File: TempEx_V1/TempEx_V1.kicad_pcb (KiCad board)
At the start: 2 copper layers, 25 parts, among them J1 Conn_01x02, J2 Conn_01x10, J3 Conn_01x02, J4 Conn_01x02, J5 Conn_01x02, U1 MAX31865xTP, U2 MAX31865xTP, U3 MAX31865xTP, U4 MAX31865xTP

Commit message: WIP
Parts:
- moved C4 95.2 mm to (145.2, 118.8), turned to -90 degrees
- moved C3 94.8 mm to (145.2, 115.4), turned to 90 degrees
- moved J3 93.4 mm to (137.6, 111.1), turned to 180 degrees
- moved U2 91.0 mm to (141.3, 117.4), turned to -90 degrees
- moved C10 90.4 mm to (137.4, 117.3), turned to -90 degrees
- moved R2 89.2 mm to (141.6, 113.8), turned to 180 degrees
- moved J1 74.8 mm to (117.7, 111.2), turned to 180 degrees
- moved C1 72.3 mm to (125.2, 115.4), turned to 90 degrees
- moved C2 71.9 mm to (125.2, 118.8), turned to -90 degrees
- moved J5 68.4 mm to (142.3, 138.8)
- moved R4 68.1 mm to (138.4, 136.2)
- moved R1 65.4 mm to (121.6, 113.8), turned to 180 degrees
- moved C12 63.8 mm to (142.6, 132.6), turned to 90 degrees
- moved C7 63.7 mm to (134.8, 134.6), turned to -90 degrees
- moved C9 63.3 mm to (117.4, 117.4), turned to -90 degrees
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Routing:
- net +3V3: track 0.00 -> 176.8 mm
- net /Temperature/SPI_MOSI: track 0.00 -> 63.0 mm, vias 0 -> 4
- net /Temperature/SPI_NSS1: track 0.00 -> 56.9 mm
- net /Temperature/SPI_MISO: track 0.00 -> 55.4 mm, vias 0 -> 6
- net /Temperature/SPI_CLK: track 0.00 -> 55.0 mm, vias 0 -> 5
- net /Temperature/SPI_NSS2: track 0.00 -> 40.1 mm, vias 0 -> 2
- net /Temperature/SPI_NSS4: track 0.00 -> 35.8 mm
- net GND: track 0.00 -> 35.7 mm, vias 0 -> 8
- net /Temperature/SPI_NSS3: track 0.00 -> 18.8 mm
- net Net-(C11-Pad1): track 0.00 -> 11.9 mm
- net Net-(C10-Pad1): track 0.00 -> 11.9 mm
- net Net-(C9-Pad1): track 0.00 -> 11.8 mm
- net Net-(C12-Pad1): track 0.00 -> 11.8 mm
- net Net-(C11-Pad2): track 0.00 -> 10.7 mm
- net GNDD: track 0.00 -> 10.7 mm
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- added copper zone on B.Cu, net GND
- added copper zone on F.Cu, net GND
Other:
- board outline added: 50 x 40 mm
- board text added: "Temp1"
- board text added: "Temp2"
- board text added: "Temp3"
- board text added: "Temp4"

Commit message: GNDD Problem still unresolved
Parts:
- R1, R2, R3, R4: footprint Resistor_SMD:R_0201_0603Metric_Pad0.64x0.40mm_HandSolder -> Resistor_SMD:R_0603_1608Metric_Pad0.98x0.95mm_HandSolder
- moved R3 0.93 mm to (117.5, 136.6)
- moved R4 0.84 mm to (137.6, 136.5)
- moved R1 0.80 mm to (122.3, 113.5)
- moved R2 0.79 mm to (142.3, 113.5)
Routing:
- net +3V3: track 176.8 -> 175.5 mm
- net Net-(R3-Pad1): track 1.84 -> 2.52 mm
- net Net-(C9-Pad2): track 10.1 -> 10.7 mm
- net Net-(R4-Pad1): track 1.83 -> 2.43 mm
- net Net-(R2-Pad1): track 1.84 -> 2.43 mm
- net Net-(R1-Pad1): track 1.84 -> 2.41 mm
- net GND: vias 8 -> 12

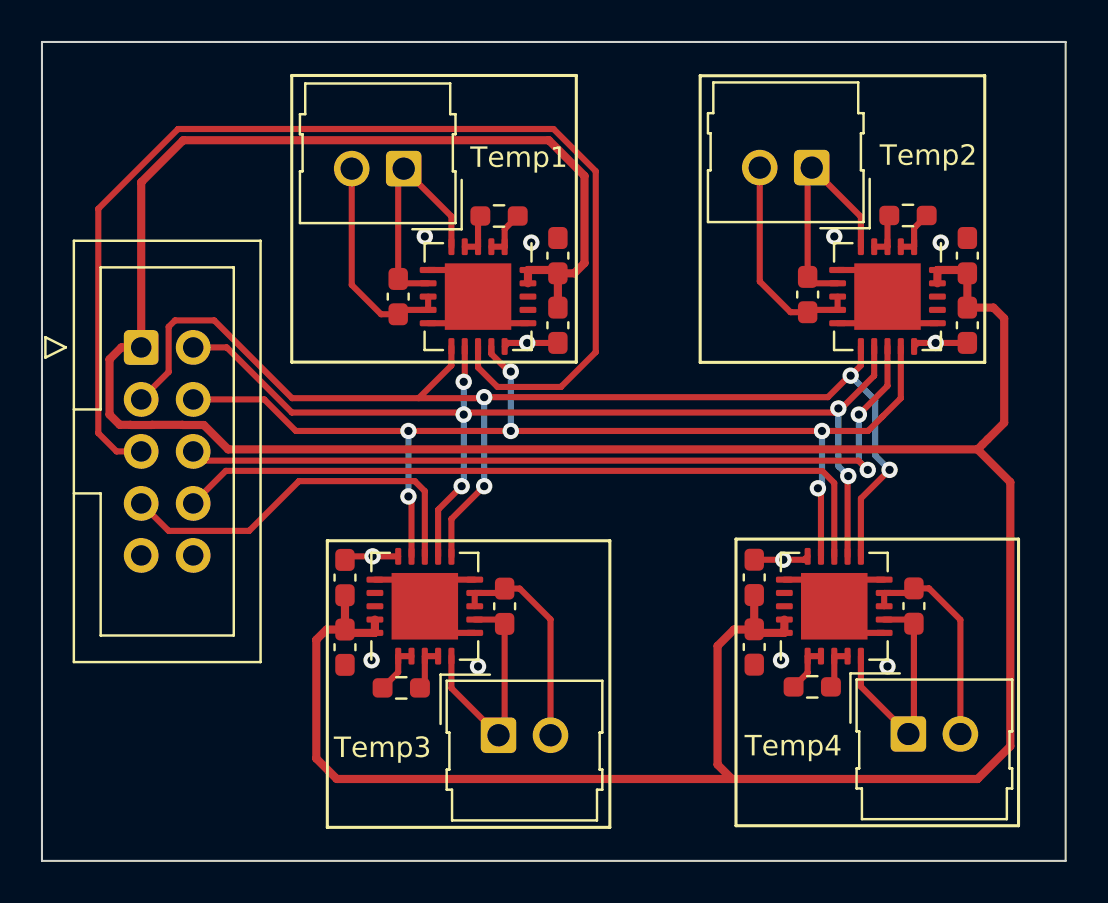
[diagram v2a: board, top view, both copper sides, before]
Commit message: Stitching missing
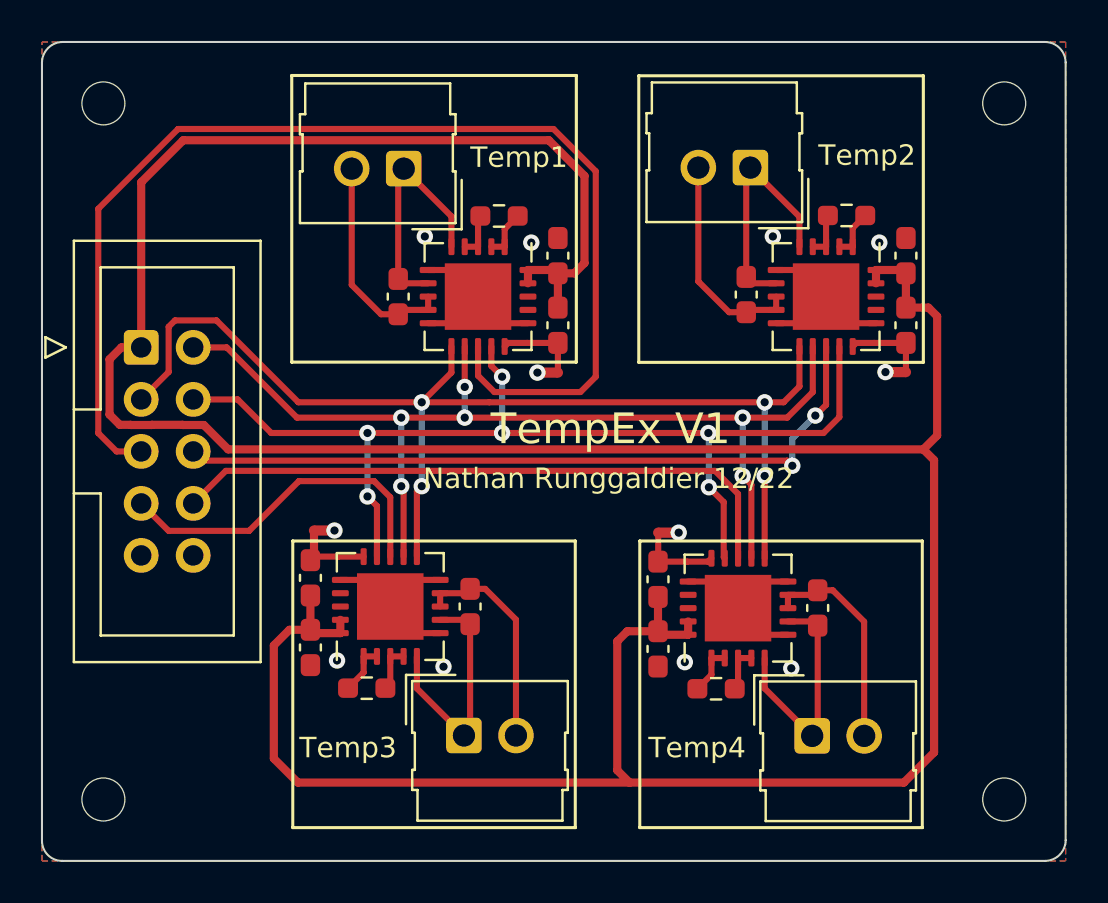
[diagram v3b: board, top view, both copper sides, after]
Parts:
- added H1: MountingHole, MountingHole:MountingHole_2.1mm, F.Cu at (103.0, 108.0)
- added H2: MountingHole, MountingHole:MountingHole_2.1mm, F.Cu at (103.0, 142.0)
- added H3: MountingHole, MountingHole:MountingHole_2.1mm, F.Cu at (147.0, 142.0)
- added H4: MountingHole, MountingHole:MountingHole_2.1mm, F.Cu at (147.0, 108.0)
- added NT1: NetTie_2, NetTie:NetTie-2_SMD_Pad0.5mm, F.Cu at (124.7, 121.2)
- added NT2: NetTie_2, NetTie:NetTie-2_SMD_Pad0.5mm, F.Cu at (141.7, 121.1)
- added NT3: NetTie_2, NetTie:NetTie-2_SMD_Pad0.5mm, F.Cu at (113.8, 128.9)
- added NT4: NetTie_2, NetTie:NetTie-2_SMD_Pad0.5mm, F.Cu at (130.6, 129.0)
- moved C12 4.70 mm to (137.9, 132.6)
- moved C7 4.70 mm to (130.1, 134.6)
- moved C8 4.70 mm to (130.1, 131.2)
- moved J5 4.70 mm to (137.6, 138.9)
- moved R4 4.70 mm to (132.9, 136.6)
- moved U4 4.70 mm to (134.0, 132.7)
- moved C10 3.00 mm to (134.4, 117.3)
- moved C3 3.00 mm to (142.2, 115.4)
- moved C4 3.00 mm to (142.2, 118.8)
- moved J3 3.00 mm to (134.6, 111.1)
- moved R2 3.00 mm to (139.3, 113.5)
- moved U2 3.00 mm to (138.3, 117.4)
- moved C11 1.69 mm to (120.9, 132.6)
- moved C5 1.69 mm to (113.1, 134.6)
- moved C6 1.69 mm to (113.1, 131.2)
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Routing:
- net GNDD: track 10.7 -> 16.3 mm
- net /Temperature/SPI_MOSI: track 63.0 -> 57.6 mm
- net /Temperature/SPI_NSS4: track 35.8 -> 30.9 mm
- net +3V3: track 175.5 -> 171.3 mm
- net /Temperature/SPI_NSS2: track 40.1 -> 36.1 mm
- net /Temperature/SPI_CLK: track 55.0 -> 51.8 mm, vias 5 -> 6
- net /Temperature/SPI_MISO: track 55.4 -> 53.1 mm
- net /Temperature/SPI_NSS3: track 18.8 -> 17.0 mm
- net /Temperature/SPI_NSS1: track 56.9 -> 58.0 mm
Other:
- outline, holes or cut-outs redrawn
- board text added: "Nathan Runggaldier 12/22"
- board text added: "TempEx V1"

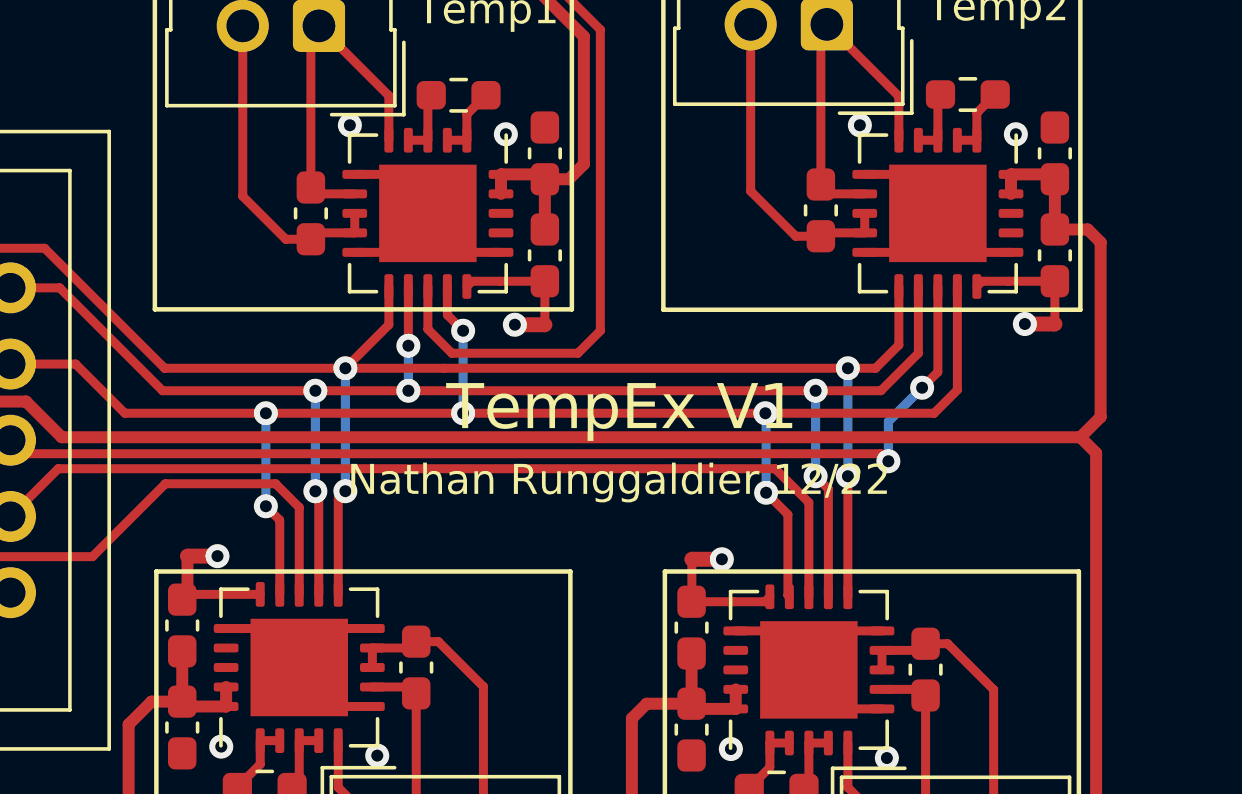
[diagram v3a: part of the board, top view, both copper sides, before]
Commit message: Updated GND
All GNDD switched to GND
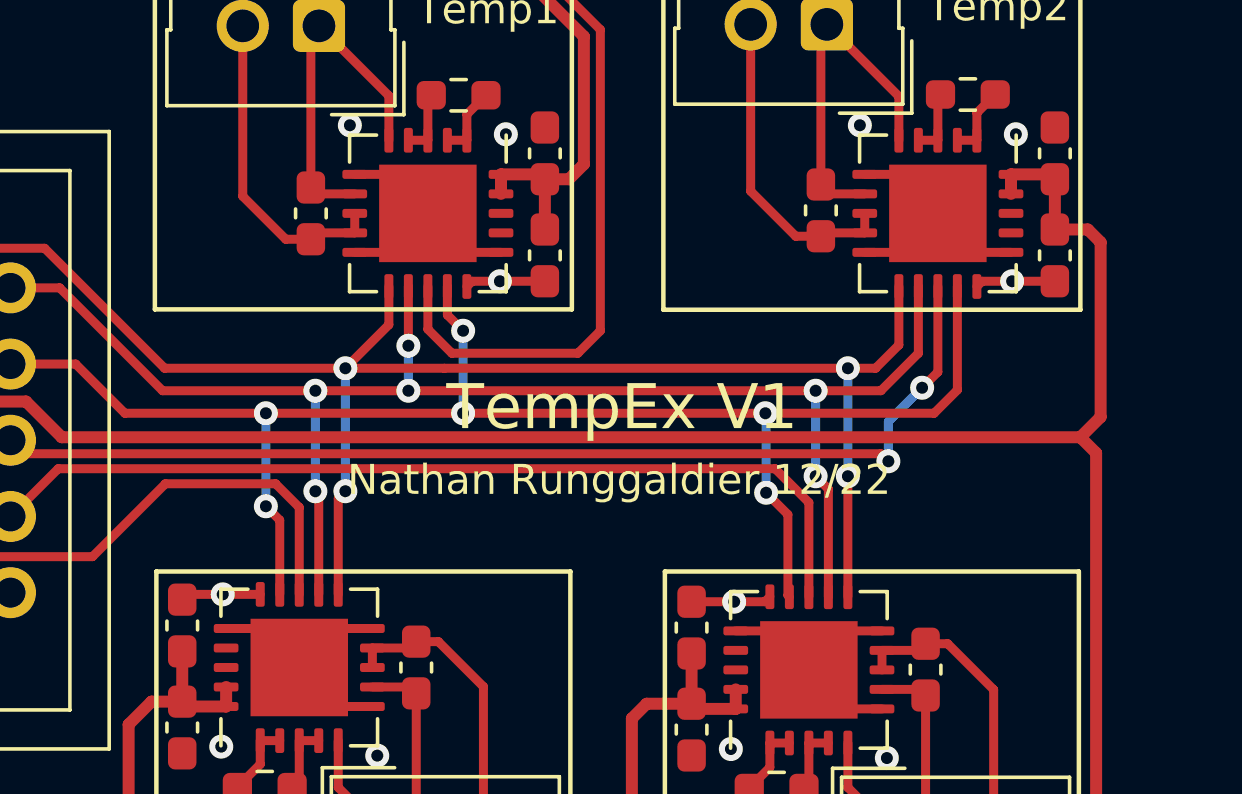
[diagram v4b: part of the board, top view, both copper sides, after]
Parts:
- removed NT1, NT2, NT3, NT4: NetTie_2, NetTie:NetTie-2_SMD_Pad0.5mm
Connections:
- C2 pad 2: GNDD -> GND
- C4 pad 2: GNDD -> GND
- C6 pad 2: GNDD -> GND
- C8 pad 2: GNDD -> GND
- U1 pad 15: GNDD -> GND
- U2 pad 15: GNDD -> GND
- U3 pad 15: GNDD -> GND
- U4 pad 15: GNDD -> GND
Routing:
- net GNDD: track 16.3 -> 0.00 mm
- net GND: track 35.7 -> 46.4 mm

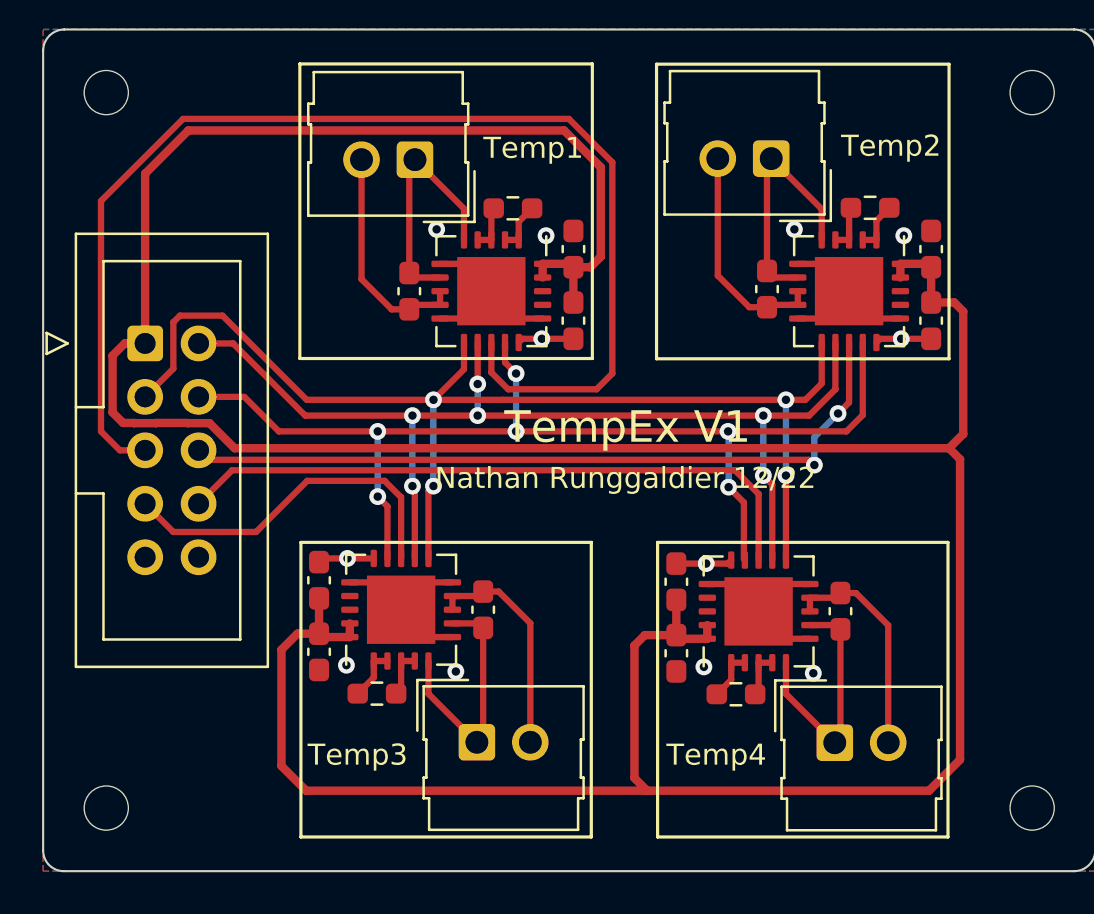
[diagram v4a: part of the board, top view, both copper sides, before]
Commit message: Change from 2 layers to 4
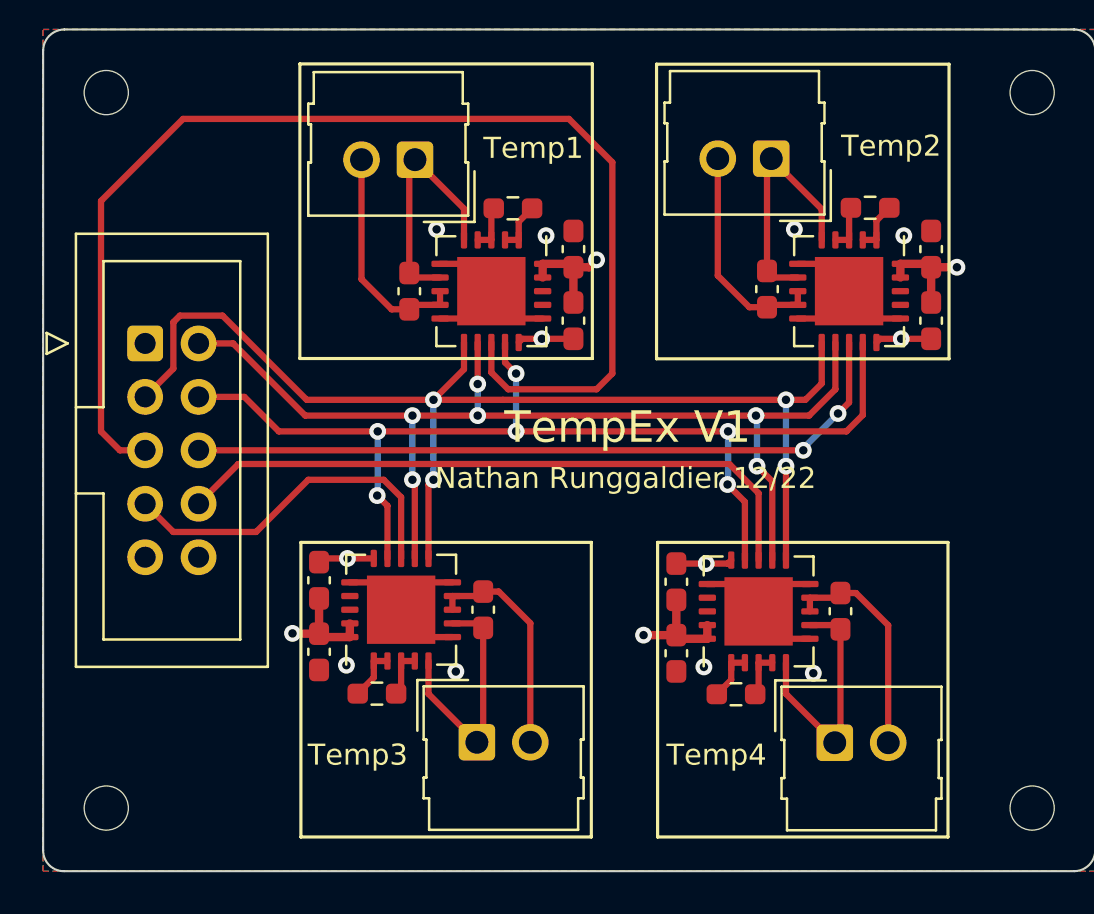
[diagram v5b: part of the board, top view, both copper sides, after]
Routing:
- net +3V3: track 171.3 -> 20.7 mm, vias 0 -> 4
- net /Temperature/SPI_NSS2: track 36.1 -> 34.8 mm
- added copper zone on In1.Cu, net +3V3
- added copper zone on In2.Cu, net GND
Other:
- copper layers 2 -> 4
